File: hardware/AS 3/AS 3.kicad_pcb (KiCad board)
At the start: 4 copper layers, 45 x 95 mm, 12 parts, among them J1 Conn_02x03_Odd_Even, J3 Connector, USB-TYPE-C-16P, U1 ESP32-S3-WROOM-1

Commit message: PCB done????
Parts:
- added BOOT: SW_Push, Button_Switch_SMD:SW_SPST_Omron_B3FS-100xP, F.Cu at (89.1, 64.6)
- added C1: 100nF, Capacitor_SMD:C_0402_1005Metric, F.Cu at (85.3, 112.8)
- added C10: 22uF, Capacitor_SMD:C_1206_3216Metric, F.Cu at (86.7, 87.5)
- added C11: 4.7uF, Capacitor_SMD:C_1206_3216Metric, F.Cu at (74.9, 60.0)
- added C12: 100nF, Capacitor_SMD:C_0603_1608Metric, F.Cu at (79.0, 59.6)
- added C13: 47uF, Capacitor_SMD:CP_Elec_6.3x5.7, F.Cu at (76.9, 54.9)
- added C14: 100nF, Capacitor_SMD:C_0603_1608Metric, F.Cu at (66.0, 86.3)
- added C15: 10uF, Capacitor_SMD:C_0805_2012Metric, F.Cu at (66.3, 84.4)
- added C16: 100nF, Capacitor_SMD:C_0603_1608Metric, F.Cu at (79.1, 65.1)
- added C17: 18nF, Capacitor_SMD:C_0603_1608Metric, F.Cu at (63.5, 89.6)
- added C18: 22uF, Capacitor_SMD:C_0805_2012Metric, F.Cu at (69.2, 88.8)
- added C19: 22uF, Capacitor_SMD:C_1206_3216Metric, F.Cu at (61.1, 53.7)
- added C2: 1uF, Capacitor_SMD:C_0402_1005Metric, F.Cu at (83.4, 111.0)
- added C20: 10nF, Capacitor_SMD:C_0402_1005Metric, F.Cu at (83.0, 112.8)
- added C21: 100nF, Capacitor_SMD:C_0402_1005Metric, F.Cu at (84.1, 112.8)
- added C22: 22uF, Capacitor_SMD:C_1206_3216Metric, F.Cu at (86.7, 84.7)
- added C23: 100nF, Capacitor_SMD:C_0402_1005Metric, F.Cu at (83.1, 55.5)
- added C24: 10uF, Capacitor_SMD:C_0805_2012Metric, F.Cu at (84.8, 56.3)
- added C25: 10uF, Capacitor_SMD:C_0805_2012Metric, F.Cu at (67.2, 73.7)
- added C26: 100nF, Capacitor_SMD:C_0603_1608Metric, F.Cu at (69.3, 73.8)
- added C27: 10uF, Capacitor_SMD:C_0805_2012Metric, F.Cu at (71.0, 81.2)
- added C28: 100nF, Capacitor_SMD:C_0603_1608Metric, F.Cu at (69.0, 81.0)
- added C29: 100nF, Capacitor_SMD:C_0603_1608Metric, F.Cu at (64.5, 78.5)
- added C3: 10uF, Capacitor_SMD:C_0805_2012Metric, F.Cu at (85.4, 110.0)
- added C30: 22uF, Capacitor_SMD:C_0805_2012Metric, F.Cu at (66.2, 82.2)
- added C31: 22uF, Capacitor_SMD:C_0805_2012Metric, F.Cu at (64.2, 74.5)
- added C32: 100nF, Capacitor_SMD:C_0603_1608Metric, F.Cu at (66.5, 80.2)
- added C5: 100nF, Capacitor_SMD:C_0402_1005Metric, F.Cu at (63.5, 83.2)
- added C6: 2.2uF, Capacitor_SMD:C_0805_2012Metric, F.Cu at (70.9, 59.5)
- added C7: 22uF, Capacitor_SMD:C_0805_2012Metric, F.Cu at (71.3, 73.6)
- added C8: 22uF, Capacitor_SMD:C_0805_2012Metric, F.Cu at (69.1, 85.1)
- added C9: 22uF, Capacitor_SMD:C_1206_3216Metric, F.Cu at (74.9, 62.7)
- added D10: D_TVS_Small, Diode_SMD:D_SOD-882, F.Cu at (84.1, 96.8)
- added D11: D_TVS_Small, Diode_SMD:D_SOD-882, F.Cu at (84.6, 94.4)
- added D2_1: SMBJ28A, PCM_JLCPCB:D_SMB, F.Cu at (68.3, 64.1)
- added D2_2: SMBJ14A, PCM_JLCPCB:D_SMB, F.Cu at (68.3, 69.0)
- added D4: Green, LED_SMD:LED_0603_1608Metric, F.Cu at (56.1, 85.2)
- added D5: Green, LED_SMD:LED_0603_1608Metric, F.Cu at (56.1, 82.4)
- added D6: Green, LED_SMD:LED_0603_1608Metric, F.Cu at (56.1, 90.3)
- added D7: Green, LED_SMD:LED_0603_1608Metric, F.Cu at (56.2, 93.0)
- added D8: D_TVS_Small, Diode_SMD:D_SOD-882, F.Cu at (52.8, 72.4)
- added D9: WS2812B, PCM_JLCPCB:LED-SMD_4P-L1.6-W1.5_XL-1615RGBC-WS2812B, F.Cu at (56.2, 95.6)
- added L1: 10uH, Inductor_SMD:L_Chilisin_BMRF00101040, F.Cu at (78.3, 73.1)
- added L2: 2.2uH, Inductor_SMD:L_Chilisin_BMRF00101040, F.Cu at (78.3, 87.1)
- added Q1: PSMN5R2-60YL, Package_TO_SOT_SMD:LFPAK56, F.Cu at (67.6, 54.2)
- added R1: 100K, Resistor_SMD:R_0402_1005Metric, F.Cu at (86.4, 58.8)
- added R10: 86.6kΩ, Resistor_SMD:R_0402_1005Metric, F.Cu at (65.0, 77.2)
- added R11: 1K, Resistor_SMD:R_0402_1005Metric, F.Cu at (59.3, 87.7)
- added R12: 10K, Resistor_SMD:R_0402_1005Metric, F.Cu at (71.0, 77.2)
- added R13: 4,7K, Resistor_SMD:R_0402_1005Metric, F.Cu at (71.0, 78.4)
- added R14: 86.6kΩ, Resistor_SMD:R_0402_1005Metric, F.Cu at (81.8, 60.8)
- added R15: 100K, Resistor_SMD:R_0402_1005Metric, F.Cu at (81.8, 58.1)
- added R16: 16K, Resistor_SMD:R_0402_1005Metric, F.Cu at (81.8, 59.5)
- added R17: 4.7K, Resistor_SMD:R_0402_1005Metric, F.Cu at (84.2, 60.0)
- added R18: 100K, Resistor_SMD:R_0402_1005Metric, F.Cu at (84.2, 61.3)
- added R19: 61.9K, Resistor_SMD:R_0402_1005Metric, F.Cu at (63.8, 86.9)
- added R2: 1K, Resistor_SMD:R_0402_1005Metric, F.Cu at (59.2, 85.2)
- added R20: 220, Resistor_SMD:R_0402_1005Metric, F.Cu at (59.3, 93.0)
- added R21: 1K, Resistor_SMD:R_0402_1005Metric, F.Cu at (59.2, 90.3)
- added R22: 10K, Resistor_SMD:R_0402_1005Metric, F.Cu at (63.2, 76.7)
- added R5: 4.7K, Resistor_SMD:R_0402_1005Metric, F.Cu at (59.3, 82.5)
- added R6: 4.7K, Resistor_SMD:R_0402_1005Metric, F.Cu at (84.2, 58.8)
- added R7: 10K, Resistor_SMD:R_0402_1005Metric, F.Cu at (84.2, 62.5)
- added R8: 1K, Resistor_SMD:R_0603_1608Metric, F.Cu at (63.5, 81.0)
- added R9: 2K, Resistor_SMD:R_0402_1005Metric, F.Cu at (63.5, 84.3)
- added RESET: SW_Push, Button_Switch_SMD:SW_SPST_Omron_B3FS-100xP, F.Cu at (89.0, 75.3)
- added U2: LM74610QDGKTQ1, LM74610QDGKTQ1:SOP65P490X110-8N, F.Cu at (66.0, 59.5)
- added U3: LMR604205SRAKRQ1, LMR60420:RAK0009A-MFG, F.Cu at (79.1, 62.3)
- added U4: TPS62901RPJR, TPS62901:QFN_902RPJR_TEX, F.Cu at (66.0, 88.7)
- added U5: BME280, BME280:PSON65P250X250X100-8N, F.Cu at (84.2, 52.8)
- added U6: TPS2121RUXR, TPS2121RUXR:IC_TPS2121RUXR, F.Cu at (68.0, 77.8)
- added UART: Conn_01x04, Connector_Molex:Molex_CLIK-Mate_502382-0470_1x04-1MP_P1.25mm_Vertical, F.Cu at (56.0, 101.8)
- D1: value ESD321DYAR -> Green; footprint PCM_JLCPCB:D_SOD-523 -> LED_SMD:LED_0603_1608Metric
- D2: value ESD321DYAR -> D_TVS_Small; footprint PCM_JLCPCB:D_SOD-523 -> Diode_SMD:D_SOD-882
- D3: value ESD441DPLR -> D_TVS_Small; footprint PCM_JLCPCB:D_SOD-123FL -> Diode_SMD:D_SOD-882
- R3, R4: footprint PCM_JLCPCB:R_0603 -> Resistor_SMD:R_0402_1005Metric
- USB-C: renamed from J3; value Connector, USB-TYPE-C-16P -> USB_C_Receptacle_USB2.0_16P; footprint PCM_JLCPCB:TYPE-C-SMD_HX-TYPE-C-16PIN -> Connector_USB:USB_C_Receptacle_HRO_TYPE-C-31-M-12
- moved D2 62.6 mm to (63.5, 72.4)
- moved R3 52.4 mm to (89.1, 91.2), turned to 180 degrees
- moved D1 48.2 mm to (56.1, 87.7), turned to 0 degrees
- moved USB-C 48.2 mm to (90.8, 97.2), turned to 90 degrees
- moved R4 46.6 mm to (89.0, 103.2), turned to 180 degrees
- moved D3 42.9 mm to (84.1, 98.7), turned to -90 degrees
- moved H3 30.0 mm to (90.0, 110.0)
- moved H4 30.0 mm to (55.0, 110.0)
- moved J1 21.6 mm to (57.8, 67.2), turned to -90 degrees
- moved U1 19.5 mm to (72.4, 108.3), turned to 180 degrees
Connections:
- D1 pad 1: /D- -> GND
- D1 pad 2: GND -> Net-(D1-A)
- D2 pad 1: /D+ -> +5VMUX
- D3 pad 1: VBUS -> /D-
- J1 pad 3: unconnected-(J1-Pin_3-Pad3) -> +5VMUX
- J1 pad 4: /PX3_Signal -> GND
- J1 pad 5: +5V -> unconnected-(J1-Pin_5-Pad5)
- J1 pad 6: GND -> /PX3_Signal
- J1 pad MP: (no net) -> GND
- U1 pad 2: VDD33 -> +3.3V
- U1 pad 26: unconnected-(U1-IO45-Pad26) -> /PX3_PRESS
- U1 pad 28: unconnected-(U1-IO35-Pad28) -> /LED
- U1 pad 34: /PX3_PRESS -> unconnected-(U1-IO41-Pad34)
- U1 pad 5: /LED -> unconnected-(U1-IO5-Pad5)
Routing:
- net /SDA: track 0.00 -> 59.7 mm, vias 0 -> 2
- net /EN: track 0.00 -> 59.2 mm
- net /SCL: track 0.00 -> 57.0 mm, vias 0 -> 2
- net /BOOT: track 0.00 -> 52.0 mm, vias 0 -> 2
- net +5VBus: track 0.00 -> 50.3 mm, vias 0 -> 10
- net /PG: track 0.00 -> 38.9 mm, vias 0 -> 2
- net GND: track 10.2 -> 42.4 mm, vias 4 -> 101
- net +12VA: track 0.00 -> 31.6 mm, vias 0 -> 6
- net +3.3V: track 0.00 -> 28.1 mm, vias 0 -> 20
- net +5VMUX: track 0.00 -> 23.9 mm, vias 0 -> 10
- net +5V: track 0.00 -> 16.9 mm, vias 0 -> 1
- net /PX3_Signal: track 0.00 -> 16.6 mm
- net /PX3_PRESS: track 0.00 -> 16.3 mm
- net Net-(U4-SW): track 0.00 -> 13.3 mm
- net /TXD0: track 0.00 -> 11.9 mm
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- added copper zone on F.Cu, net +12V
- added copper zone on In2.Cu, net +12V
- added copper zone on F.Cu, net +12VA
- added copper zone on In2.Cu, net +12VA
- added copper zone on F.Cu, net +3.3V
- added copper zone on In2.Cu, net +3.3V
- added copper zone on F.Cu, net +5V
- added copper zone on In2.Cu, net +5VBus
- added copper zone on In2.Cu, net +5VMUX
- added copper zone on F.Cu, net GND
- added copper zone on In1.Cu, net GND
- removed copper zone on B.Cu, net GND
- removed copper zone on In2.Cu, net VBUS
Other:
- board size 45 x 95 mm -> 45 x 65 mm
- board text added: "+"
- board text added: "+5V"
- board text added: "+5V-"
- board text added: "12V"
- board text added: "12V-"
- board text added: "3V3"
- board text added: "5V"
- board text added: "AIR SCALES"
- board text added: "PX3"
- board text added: "SYS"
- board text added: "USB"
- board text added: "V3"

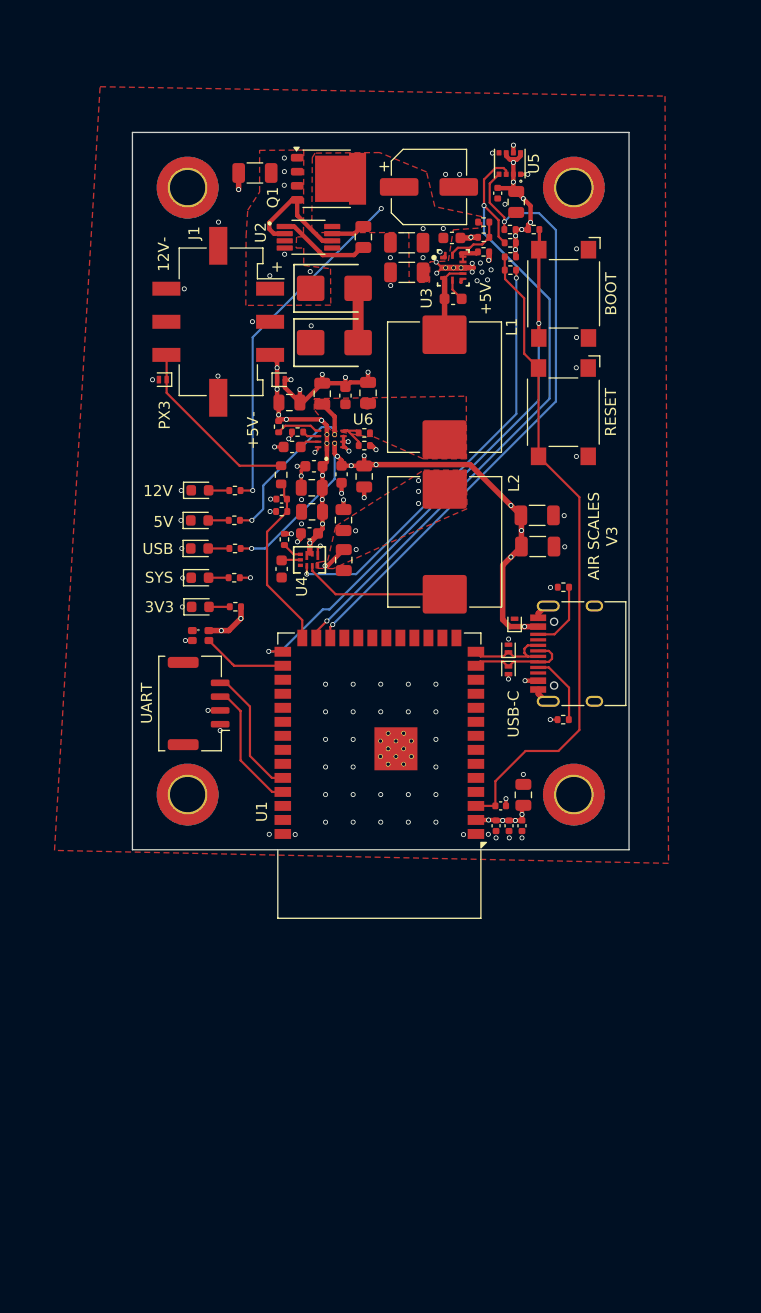
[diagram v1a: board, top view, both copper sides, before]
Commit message: time to make vias bigger and order this thing
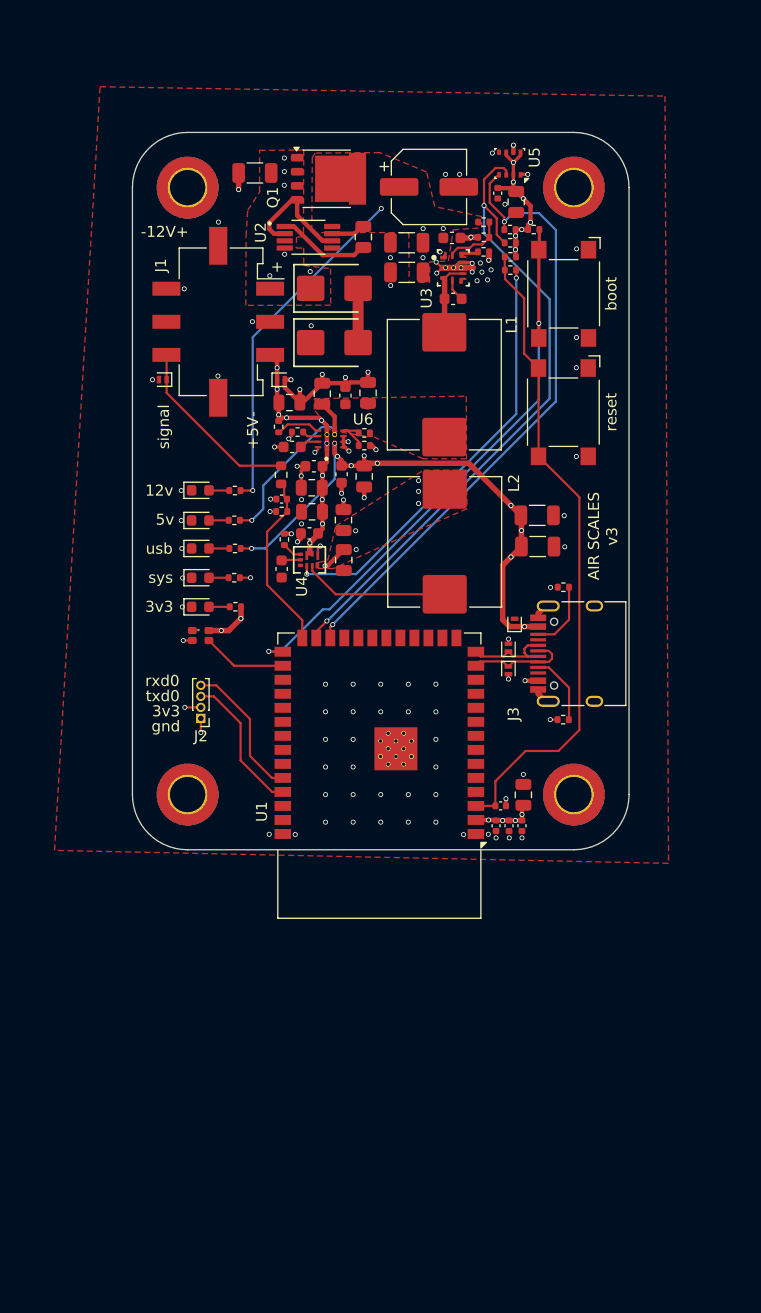
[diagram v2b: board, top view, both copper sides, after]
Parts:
- C24: value 10uF -> 10u
- D1, D4, D5, D6, D7: value Green -> LED_Small
- J2: renamed from UART; footprint Connector_Molex:Molex_CLIK-Mate_502382-0470_1x04-1MP_P1.25mm_Vertical -> Connector_PinHeader_1.00mm:PinHeader_1x04_P1.00mm_Vertical
- R17, R6: value 4.7K -> 1k
- U5: footprint BME280:PSON65P250X250X100-8N -> Package_LGA:Bosch_LGA-8_2.5x2.5mm_P0.65mm_ClockwisePinNumbering
- moved J2 1.36 mm to (56.2, 103.1), turned to 180 degrees
- moved L1 0.22 mm to (78.3, 72.9)
- moved D10 0.09 mm to (84.1, 96.7)
- moved D1 0.08 mm to (56.2, 87.7)
- moved D4 0.07 mm to (56.2, 85.2)
- turned U5 to 180 degrees
- renumbered USB-C to J3, RESET to SW1, BOOT to SW2
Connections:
- R14 pad 1: Net-(U3-MODE_SYNC) -> Net-(U3-RT)
- U3 pad 7: Net-(U3-MODE_SYNC) -> GND
- U3 pad 8: Net-(U3-MODE_SYNC) -> Net-(U3-RT)
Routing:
- net GND: track 42.4 -> 47.7 mm
- net Net-(U3-MODE_SYNC): track 2.46 -> 0.00 mm
- net Net-(U3-RT): track 0.00 -> 1.86 mm
- net /TXD0: track 11.9 -> 13.0 mm
- net /RXD0: track 11.9 -> 12.9 mm
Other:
- outline, holes or cut-outs redrawn
- board text added: "-12V+"
- board text added: "12v"
- board text added: "3v3"
- board text added: "5v"
- board text added: "boot"
- board text added: "gnd"
- board text added: "reset"
- board text added: "rxd0"
- board text added: "signal"
- board text added: "sys"
- board text added: "txd0"
- board text added: "usb"
- board text added: "v3"
- board text removed: "+5V"
- board text removed: "12V"
- board text removed: "12V-"
- board text removed: "3V3"
- board text removed: "5V"
- board text removed: "PX3"
- board text removed: "SYS"
- board text removed: "USB"
- board text removed: "V3"

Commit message: almost ready now
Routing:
- net GND: track 47.7 -> 54.0 mm
- net Net-(U3-FB): track 6.95 -> 11.9 mm
- net +5VBus: track 50.4 -> 52.7 mm, vias 10 -> 9
- net /PG: track 38.9 -> 39.6 mm
- net +3.3V: vias 20 -> 19
- net +12VA: vias 6 -> 5
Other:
- board text added: "mux"
- board text added: "x"
